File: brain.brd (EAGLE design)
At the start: 100 x 80 mm, 9 parts, among them IC1 MCP1253-33X50

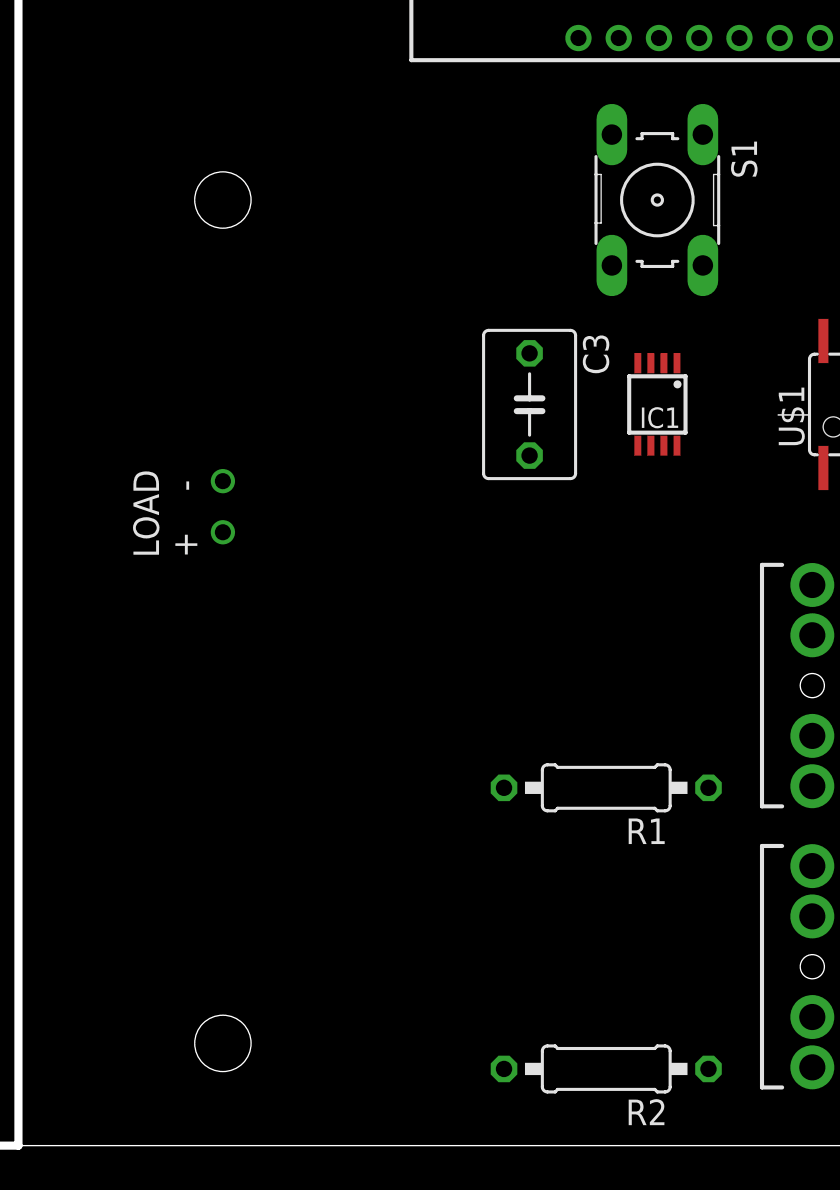
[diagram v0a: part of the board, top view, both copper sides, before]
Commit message: Changed to using the TI LDO for the voltage regulation. Created and added symbol for the Sunny Buddy mounting to allow routing tools to see the electrical connections.
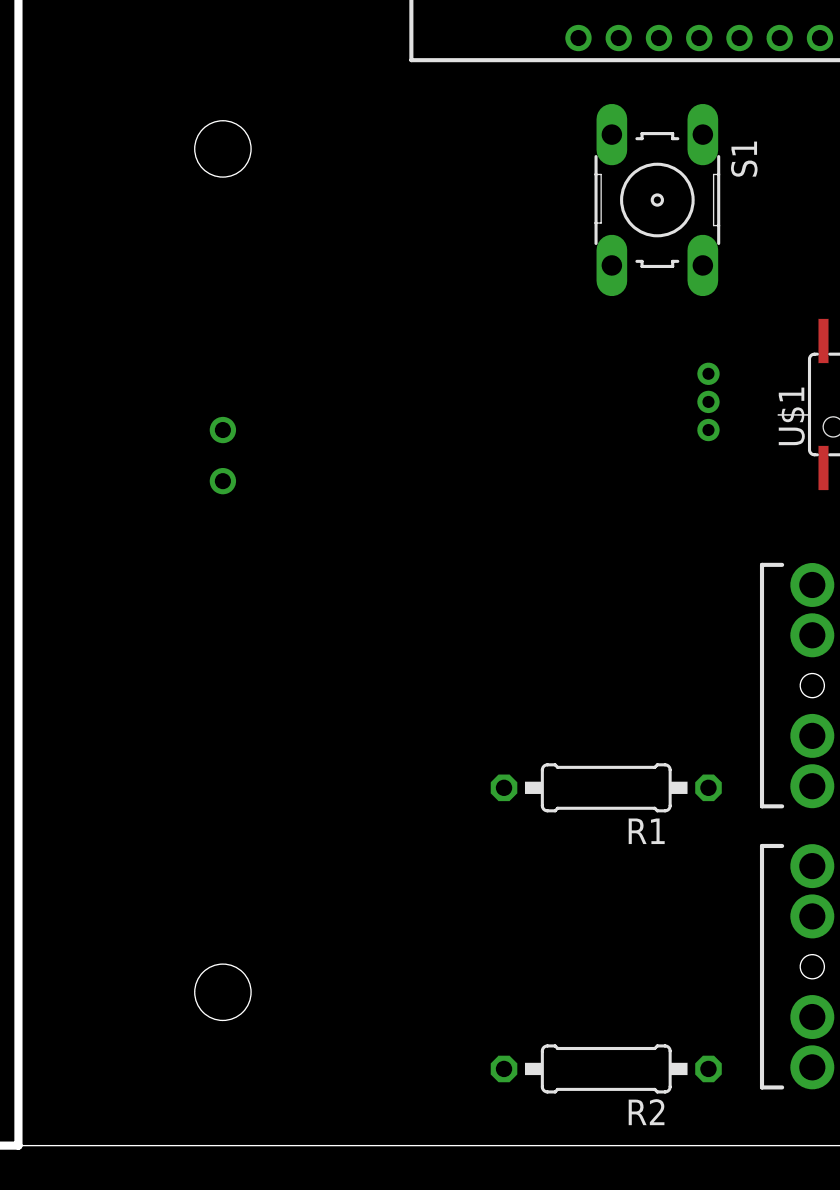
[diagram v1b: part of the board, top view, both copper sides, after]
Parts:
- removed C3: 10uF, rcl:C050-045X075
- removed IC1: MCP1253-33X50, microchip-MCP125x-xxx:MSOP8
- added U$2: LP2950, seniordesign:LP2950
- added U$3: SUNNYBUDDYMOUNT, seniordesign:SUNNYBUDDYMOUNT
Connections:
- removed net BAT: IC1.3, IC1.7, IC1.8
- removed net N$1: IC1.2, U$1.8, XB1.1
- removed net N$10: C3.1, IC1.6
- removed net N$12: C3.2, IC1.5
- removed net N$5: IC1.4, R1.2, R2.2, S1.2
- new net +3V3: U$1.8, U$2.VOUT, XB1.1
- new net VIN: U$2.VIN, U$3.P$1
- net GND: now also R1.2, R2.2, S1.2, U$2.GND, U$3.P$2
- net N$14: now also U$1.2
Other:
- board text removed: "LOAD + -"
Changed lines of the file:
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@@
 <wire x1="100" y1="80" x2="0" y2="80" width="0" layer="20"/>
 <wire x1="0" y1="80" x2="0" y2="0" width="0" layer="20"/>
-<hole x="60.96" y="46.99" drill="2.8"/>
-<hole x="60.96" y="5.08" drill="2.8"/>
 <wire x1="49.53" y1="0" x2="50.8" y2="0" width="0.4064" layer="20"/>
 <wire x1="50.8" y1="0" x2="50.8" y2="80.01" width="0.4064" layer="20"/>
-<text x="59.69" y="29.21" size="1.27" layer="21" rot="R90">LOAD
-+    -</text>
 </plain>
 <attributes>
@@
 </autorouter>
 <elements>
-<element name="IC1" library="microchip-MCP125x-xxx" package="MSOP8" value="MCP1253-33X50" x="82.55" y="36.83" rot="R180">
-<attribute name="OC_NEWARK" value="64R8540" x="82.55" y="36.83" size="1.778" layer="27" rot="R180" display="off"/>
-<attribute name="MPN" value="LT3652EMSE#TRPBF" x="82.55" y="36.83" size="1.778" layer="27" rot="R180" display="off"/>
-<attribute name="MF" value="" x="82.55" y="36.83" size="1.778" layer="27" rot="R180" display="off"/>
-</element>
 <element name="R1" library="resistor" package="0207/10" value="10k" x="80.01" y="17.78" rot="R180">
 <attribute name="OC_NEWARK" value="64R8539" x="80.01" y="17.78" size="1.778" layer="27" rot="R180" display="off"/>
@@
 <attribute name="OC_FARNELL" value="1337916" x="87.63" y="66.04" size="1.778" layer="27" rot="R270" display="off"/>
 </element>
-<element name="C3" library="rcl" package="C050-045X075" value="10uF" x="76.2" y="36.83" rot="R270"/>
 <element name="U2" library="SparkFun-Connectors" package="AUDIO-JACK" value="" x="95.25" y="22.86" rot="R180"/>
 <element name="U3" library="SparkFun-Connectors" package="AUDIO-JACK" value="" x="95.25" y="8.89" rot="R180"/>
+<element name="U$2" library="seniordesign" package="LP2950" value="LP2950" x="85.09" y="35.56" rot="R90"/>
+<element name="U$3" library="seniordesign" package="SUNNYBUDDYMOUNT" value="SUNNYBUDDYMOUNT" x="59.69" y="49.53"/>
 </elements>
 <signals>
@@
 <contactref element="XB1" pad="10"/>
 <contactref element="U$1" pad="4"/>
-<wire x1="94.605" y1="33.676" x2="78.63" y2="77.04" width="0" layer="19" extent="1-1"/>
-</signal>
-<signal name="BAT">
-<contactref element="IC1" pad="7"/>
-<contactref element="IC1" pad="3"/>
-<contactref element="IC1" pad="8"/>
-<wire x1="83.525" y1="34.78" x2="82.875" y2="34.78" width="0" layer="19" extent="1-1"/>
-<wire x1="82.225" y1="38.88" x2="82.875" y2="34.78" width="0" layer="19" extent="1-1"/>
-</signal>
-<signal name="N$1">
-<contactref element="IC1" pad="2"/>
-<contactref element="XB1" pad="1"/>
-<contactref element="U$1" pad="8"/>
-<wire x1="90.805" y1="39.984" x2="82.875" y2="38.88" width="0" layer="19" extent="1-1"/>
-<wire x1="96.63" y1="77.04" x2="90.805" y2="39.984" width="0" layer="19" extent="1-1"/>
+<contactref element="R1" pad="2"/>
+<contactref element="R2" pad="2"/>
+<contactref element="S1" pad="2"/>
+<contactref element="U$2" pad="GND"/>
+<contactref element="U$3" pad="P$2"/>
+<wire x1="84.8106" y1="43.7388" x2="78.63" y2="77.04" width="0" layer="19" extent="1-1"/>
+<wire x1="85.09" y1="36.957" x2="84.8106" y2="43.7388" width="0" layer="19" extent="1-1"/>
+<wire x1="94.605" y1="33.676" x2="85.09" y2="36.957" width="0" layer="19" extent="1-1"/>
+<wire x1="74.93" y1="17.78" x2="85.09" y2="36.957" width="0" layer="19" extent="1-1"/>
+<wire x1="74.93" y1="3.81" x2="74.93" y2="17.78" width="0" layer="19" extent="1-1"/>
+<wire x1="60.96" y1="35.56" x2="74.93" y2="17.78" width="0" layer="19" extent="1-1"/>
 </signal>
 <signal name="N$3">
@@
 <wire x1="93.345" y1="39.984" x2="85.09" y2="3.81" width="0" layer="19" extent="1-1"/>
 </signal>
-<signal name="N$5">
-<contactref element="IC1" pad="4"/>
-<contactref element="R1" pad="2"/>
-<contactref element="R2" pad="2"/>
-<contactref element="S1" pad="2"/>
-<wire x1="74.93" y1="17.78" x2="81.575" y2="38.88" width="0" layer="19" extent="1-1"/>
-<wire x1="74.93" y1="3.81" x2="74.93" y2="17.78" width="0" layer="19" extent="1-1"/>
-<wire x1="84.8106" y1="43.7388" x2="81.575" y2="38.88" width="0" layer="19" extent="1-1"/>
-</signal>
 <signal name="N$2">
 <contactref element="R1" pad="1"/>
@@
 <signal name="N$14">
 <contactref element="XB1" pad="2"/>
-</signal>
-<signal name="N$10">
-<contactref element="IC1" pad="6"/>
-<contactref element="C3" pad="1"/>
-<wire x1="82.225" y1="34.78" x2="76.2" y2="39.37" width="0" layer="19" extent="1-1"/>
-</signal>
-<signal name="N$12">
-<contactref element="IC1" pad="5"/>
-<contactref element="C3" pad="2"/>
-<wire x1="81.575" y1="34.78" x2="76.2" y2="34.29" width="0" layer="19" extent="1-1"/>
-</signal>
-<signal name="N$6">
-<via x="60.96" y="30.48" extent="1-16" drill="0.8"/>
-</signal>
-<signal name="N$7">
-<via x="60.96" y="33.02" extent="1-16" drill="0.8"/>
+<contactref element="U$1" pad="2"/>
+<wire x1="92.065" y1="33.676" x2="94.63" y2="77.04" width="0" layer="19" extent="1-1"/>
+</signal>
+<signal name="VIN">
+<contactref element="U$2" pad="VIN"/>
+<contactref element="U$3" pad="P$1"/>
+<wire x1="60.96" y1="33.02" x2="85.09" y2="35.56" width="0" layer="19" extent="1-1"/>
+</signal>
+<signal name="+3V3">
+<contactref element="XB1" pad="1"/>
+<contactref element="U$1" pad="8"/>
+<contactref element="U$2" pad="VOUT"/>
+<wire x1="90.805" y1="39.984" x2="96.63" y2="77.04" width="0" layer="19" extent="1-1"/>
+<wire x1="85.09" y1="38.354" x2="90.805" y2="39.984" width="0" layer="19" extent="1-1"/>
 </signal>
 </signals>
 </board>
 </drawing>
-<compatibility>
-<note version="6.3" minversion="6.2.2" severity="warning">
-Since Version 6.2.2 text objects can contain more than one line,
-which will not be processed correctly with this version.
-</note>
-</compatibility>
 </eagle>

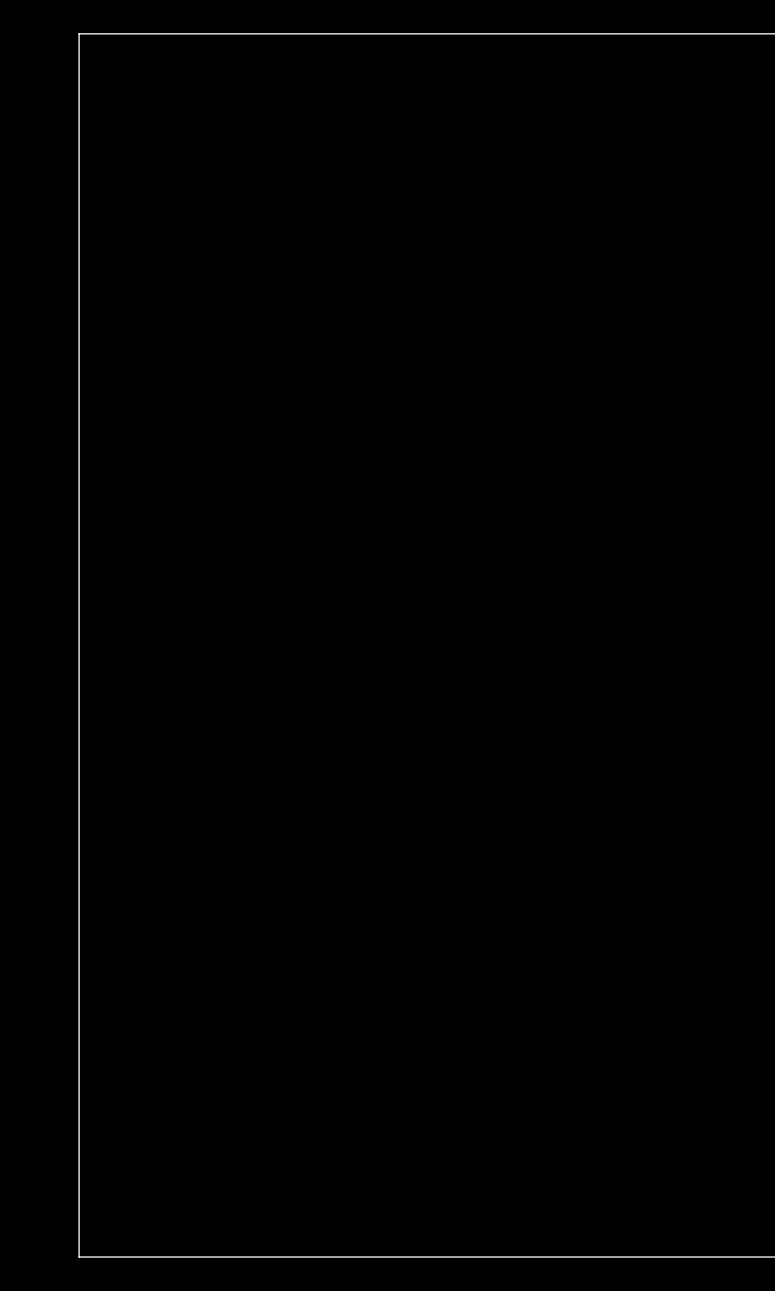
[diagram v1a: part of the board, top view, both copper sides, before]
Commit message: Added the receiver to schematic and board. Quick layout of the board.
TODO: Add bypass caps, figure out what the output of the receiver will
be (LED? something else? should we just make like through holes
for the ouput of the tiny and the supply and gnd so we can change it
on the fly?)
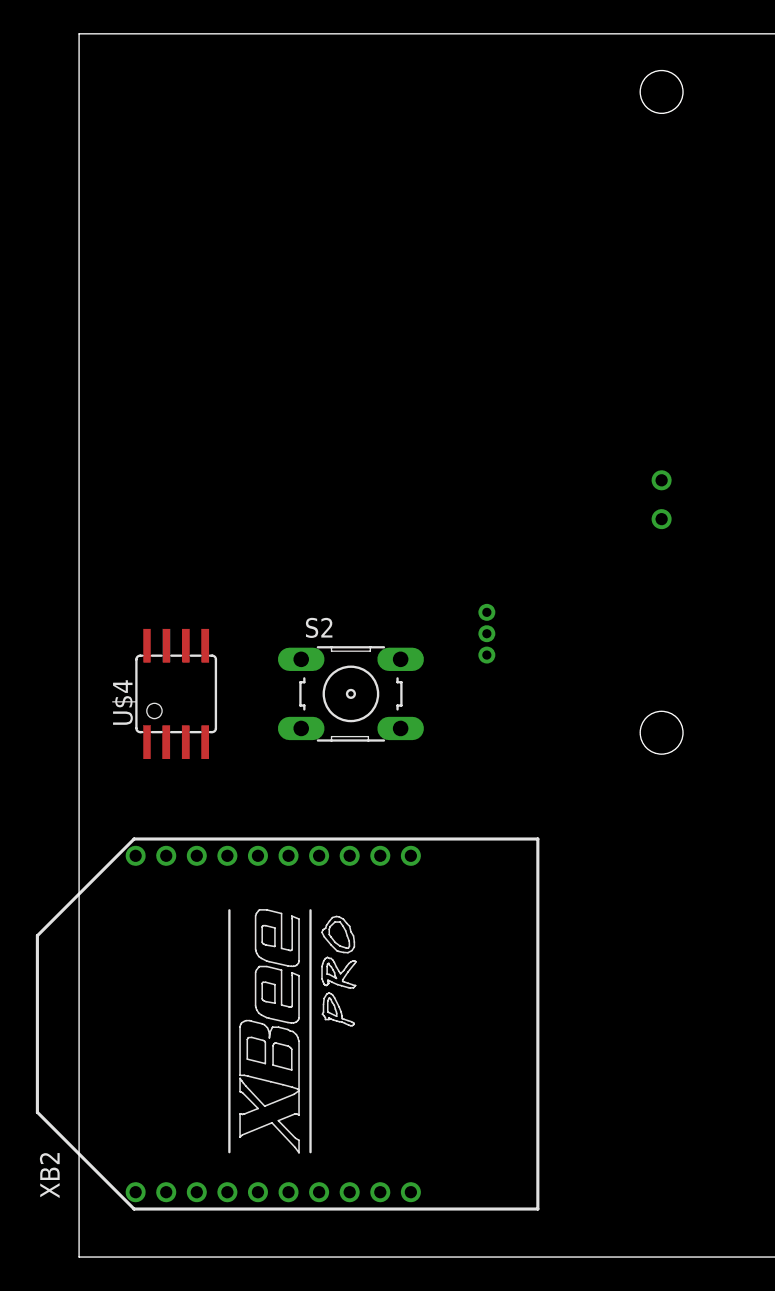
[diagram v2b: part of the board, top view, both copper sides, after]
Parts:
- added S2: (no value), switch-omron:B3F-10XX
- added U$4: ATTINY45, attiny45:SOIC8
- added U$5: LP2950, seniordesign:LP2950
- added U$6: SUNNYBUDDYMOUNT, seniordesign:SUNNYBUDDYMOUNT
- added XB2: XBEE-PRO, maxstream:XBEE-PRO
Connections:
- new net N$7: U$4.3, XB2.3
- new net N$8: S2.3, XB2.5
- new net N$9: U$4.2, XB2.2
- net +3V3: now also U$4.8, U$5.VOUT, XB2.1
- net GND: now also S2.2, U$4.4, U$5.GND, U$6.P$2, XB2.10
- net VIN: now also U$5.VIN, U$6.P$1
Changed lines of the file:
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@@
 <element name="U$2" library="seniordesign" package="LP2950" value="LP2950" x="85.09" y="35.56" rot="R90"/>
 <element name="U$3" library="seniordesign" package="SUNNYBUDDYMOUNT" value="SUNNYBUDDYMOUNT" x="59.69" y="49.53"/>
+<element name="XB2" library="maxstream" package="XBEE-PRO" value="XBEE-PRO" x="12.7" y="15.24" rot="R90">
+<attribute name="MPN" value="" x="-24.13" y="-13.97" size="1.778" layer="27" rot="R90" display="off"/>
+<attribute name="MF" value="" x="-24.13" y="-13.97" size="1.778" layer="27" rot="R90" display="off"/>
+<attribute name="OC_NEWARK" value="unknown" x="-24.13" y="-13.97" size="1.778" layer="27" rot="R90" display="off"/>
+<attribute name="OC_FARNELL" value="1337916" x="-24.13" y="-13.97" size="1.778" layer="27" rot="R90" display="off"/>
+</element>
+<element name="U$4" library="attiny45" package="SOIC8" value="ATTINY45" x="6.35" y="36.83">
+<attribute name="MPN" value="" x="-59.69" y="95.25" size="1.778" layer="27" display="off"/>
+<attribute name="MF" value="" x="-59.69" y="95.25" size="1.778" layer="27" display="off"/>
+<attribute name="OC_NEWARK" value="unknown" x="-59.69" y="95.25" size="1.778" layer="27" display="off"/>
+</element>
+<element name="S2" library="switch-omron" package="B3F-10XX" value="" x="17.78" y="36.83">
+<attribute name="MPN" value="B3F-1000" x="-29.21" y="99.06" size="1.778" layer="27" display="off"/>
+<attribute name="MF" value="" x="-29.21" y="99.06" size="1.778" layer="27" display="off"/>
+<attribute name="OC_NEWARK" value="36M3542" x="-29.21" y="99.06" size="1.778" layer="27" display="off"/>
+<attribute name="OC_FARNELL" value="176432" x="-29.21" y="99.06" size="1.778" layer="27" display="off"/>
+</element>
+<element name="U$5" library="seniordesign" package="LP2950" value="LP2950" x="26.67" y="39.37" rot="R90"/>
+<element name="U$6" library="seniordesign" package="SUNNYBUDDYMOUNT" value="SUNNYBUDDYMOUNT" x="39.37" y="34.29" rot="R180"/>
 </elements>
 <signals>
@@
 <contactref element="U$2" pad="GND"/>
 <contactref element="U$3" pad="P$2"/>
+<contactref element="XB2" pad="10"/>
+<contactref element="U$4" pad="4"/>
+<contactref element="S2" pad="2"/>
+<contactref element="U$5" pad="GND"/>
+<contactref element="U$6" pad="P$2"/>
 <wire x1="84.8106" y1="43.7388" x2="78.63" y2="77.04" width="0" layer="19" extent="1-1"/>
 <wire x1="85.09" y1="36.957" x2="84.8106" y2="43.7388" width="0" layer="19" extent="1-1"/>
@@
 <wire x1="74.93" y1="3.81" x2="74.93" y2="17.78" width="0" layer="19" extent="1-1"/>
 <wire x1="60.96" y1="35.56" x2="74.93" y2="17.78" width="0" layer="19" extent="1-1"/>
+<wire x1="8.245" y1="33.676" x2="74.93" y2="3.81" width="0" layer="19" extent="1-1"/>
+<wire x1="26.67" y1="40.767" x2="8.245" y2="33.676" width="0" layer="19" extent="1-1"/>
+<wire x1="21.0312" y1="39.0906" x2="8.245" y2="33.676" width="0" layer="19" extent="1-1"/>
+<wire x1="21.7" y1="4.24" x2="21.0312" y2="39.0906" width="0" layer="19" extent="1-1"/>
+<wire x1="38.1" y1="48.26" x2="21.7" y2="4.24" width="0" layer="19" extent="1-1"/>
 </signal>
 <signal name="N$3">
@@
 <contactref element="U$2" pad="VIN"/>
 <contactref element="U$3" pad="P$1"/>
+<contactref element="U$5" pad="VIN"/>
+<contactref element="U$6" pad="P$1"/>
 <wire x1="60.96" y1="33.02" x2="85.09" y2="35.56" width="0" layer="19" extent="1-1"/>
+<wire x1="38.1" y1="50.8" x2="60.96" y2="33.02" width="0" layer="19" extent="1-1"/>
+<wire x1="26.67" y1="39.37" x2="38.1" y2="50.8" width="0" layer="19" extent="1-1"/>
 </signal>
 <signal name="+3V3">
@@
 <contactref element="U$1" pad="8"/>
 <contactref element="U$2" pad="VOUT"/>
+<contactref element="XB2" pad="1"/>
+<contactref element="U$4" pad="8"/>
+<contactref element="U$5" pad="VOUT"/>
 <wire x1="90.805" y1="39.984" x2="96.63" y2="77.04" width="0" layer="19" extent="1-1"/>
 <wire x1="85.09" y1="38.354" x2="90.805" y2="39.984" width="0" layer="19" extent="1-1"/>
+<wire x1="3.7" y1="4.24" x2="85.09" y2="38.354" width="0" layer="19" extent="1-1"/>
+<wire x1="4.445" y1="39.984" x2="3.7" y2="4.24" width="0" layer="19" extent="1-1"/>
+<wire x1="26.67" y1="42.164" x2="4.445" y2="39.984" width="0" layer="19" extent="1-1"/>
+</signal>
+<signal name="N$7">
+<contactref element="XB2" pad="3"/>
+<contactref element="U$4" pad="3"/>
+<wire x1="7.7" y1="4.24" x2="6.975" y2="33.676" width="0" layer="19" extent="1-1"/>
+</signal>
+<signal name="N$8">
+<contactref element="XB2" pad="5"/>
+<contactref element="S2" pad="3"/>
+<wire x1="11.7" y1="4.24" x2="14.5288" y2="34.5694" width="0" layer="19" extent="1-1"/>
+</signal>
+<signal name="N$9">
+<contactref element="XB2" pad="2"/>
+<contactref element="U$4" pad="2"/>
+<wire x1="5.7" y1="4.24" x2="5.705" y2="33.676" width="0" layer="19" extent="1-1"/>
 </signal>
 </signals>
